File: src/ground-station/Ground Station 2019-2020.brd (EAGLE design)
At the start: 99.1 x 86.4 mm, 17 parts, among them U1 ADAFRUIT_RFM95W_LORA_RADIO

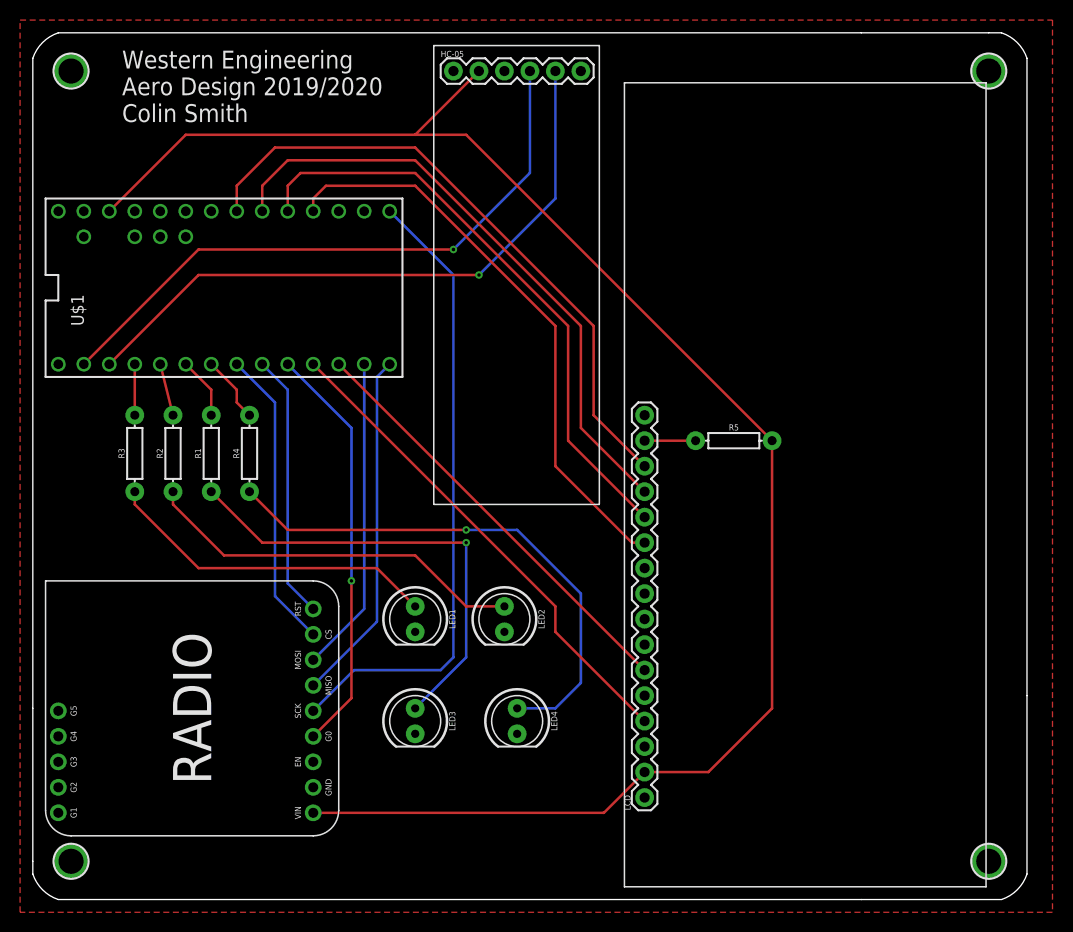
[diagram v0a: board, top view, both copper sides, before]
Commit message: Changed LCD to OLED display, changed mounting holes.
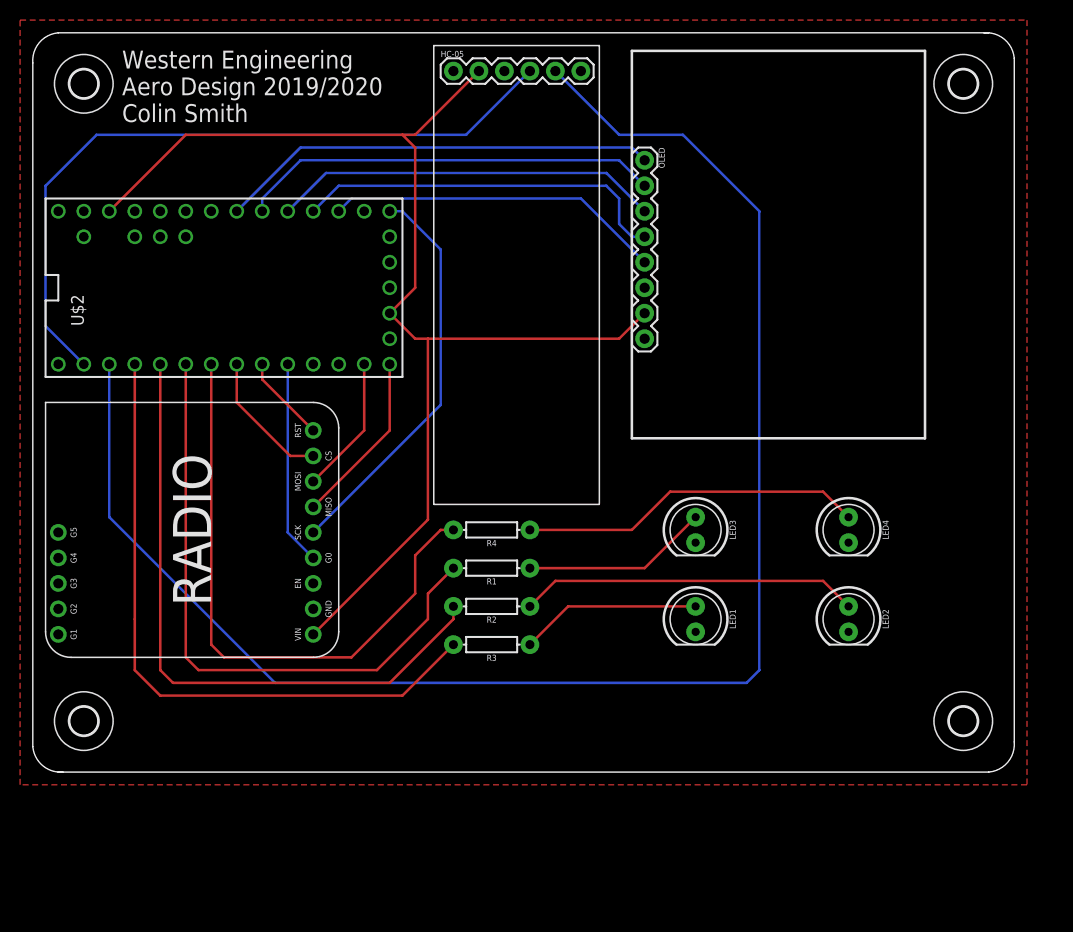
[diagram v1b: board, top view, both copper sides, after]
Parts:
- removed LCD: (no value), SparkFun-Connectors:1X16
- removed R5: 220, SparkFun-Resistors:AXIAL-0.3
- removed U$1: TEENSY_3.1-3.2_DIL+4, Teensy_3_and_LC_Series_Boards_v1.4:TEENSY_3.0-3.2&LC_DIL+4
- removed U$3, U$4, U$5: MOUNTINGHOLE2.5, microbuilder:MOUNTINGHOLE_2.5_PLATED
- added H1, H2, H3, H4: MOUNT-HOLE2.8, holes:2,8
- added OLED: (no value), SparkFun-Connectors:1X08
- U$2: value MOUNTINGHOLE2.5 -> TEENSY_3.1-3.2_ALL_PINS; device microbuilder:MOUNTINGHOLE_2.5_PLATED -> Teensy_3_and_LC_Series_Boards_v1.4:TEENSY_3.0-3.2&LC_ALL_PINS
- moved U$2 59.1 mm to (101.6, 68.6), turned to 90 degrees
- moved R3 40.3 mm to (128.3, 33.0), turned to 180 degrees
- moved LED4 38.1 mm to (163.8, 44.5)
- moved R2 35.2 mm to (128.3, 36.8), turned to 180 degrees
- moved LED2 34.3 mm to (163.8, 35.6)
- moved LED3 33.8 mm to (148.6, 44.5)
- moved R1 30.2 mm to (128.3, 40.6), turned to 180 degrees
- moved LED1 27.9 mm to (148.6, 35.6)
- moved R4 25.3 mm to (128.3, 44.5), turned to 180 degrees
- moved U1 17.8 mm to (83.8, 31.8)
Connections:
- removed net D4: LCD.11, U$1.16/A2
- removed net D5: LCD.12, U$1.17/A3
- removed net D6: LCD.13, U$1.18/A4
- removed net D7: LCD.14, U$1.19/A5
- removed net LCD_RX: LCD.4, U$1.9
- removed net LCD_TX: LCD.6, U$1.10
- removed net N$4: LCD.15, R5.P$1
- new net OLED_CLK: OLED.2, U$2.18/A4
- new net OLED_CS: OLED.5, U$2.15/A1
- new net OLED_DATA: OLED.1, U$2.19/A5
- new net OLED_DC: OLED.3, U$2.17/A3
- new net OLED_RST: OLED.4, U$2.16/A2
- new net VBAT: U$2.VBAT
- net 3.3V: now also OLED.7, U$2.3.3V, U$2.3.3V1; no longer LCD.2, R5.P$2, U$1.3.3V
- net AGND: now also U$2.AGND; no longer U$1.AGND
- net AREF: now also U$2.AREF; no longer U$1.AREF
- net CS: now also U$2.6; no longer U$1.6
- net G0: now also U$2.8; no longer U$1.8
- net GND: now also OLED.8, U$2.GND, U$2.GND1; no longer LCD.1, LCD.16, LCD.3, LCD.5, U$1.GND
- net LED1: now also U$2.2; no longer U$1.2
- net LED2: now also U$2.3; no longer U$1.3
- net LED3: now also U$2.4; no longer U$1.4
- net LED4: now also U$2.5; no longer U$1.5
- net MISO: now also U$2.12; no longer U$1.12
- net MOSI: now also U$2.11; no longer U$1.11
- net RST: now also U$2.7; no longer U$1.7
- net RX1: now also U$2.0; no longer U$1.0
- net SCK: now also U$2.13; no longer U$1.13
- net TX1: now also U$2.1; no longer U$1.1
- net VIN: now also U$2.VIN; no longer U$1.VIN
- net VUSB: now also U$2.VUSB; no longer U$1.VUSB
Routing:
- net TX1: track 64.0 -> 159.2 mm, vias 1 -> 0
- net D7: track 63.1 -> 0.00 mm
- net D6: track 61.3 -> 0.00 mm
- net LED1: track 5.08 -> 65.4 mm
- net D5: track 59.5 -> 0.00 mm
- net LED2: track 5.24 -> 64.1 mm
- net D4: track 57.7 -> 0.00 mm
- net LED3: track 6.13 -> 62.1 mm
- net LED4: track 6.66 -> 60.1 mm
- net LCD_RX: track 49.2 -> 0.00 mm
- net 3.3V: track 167.5 -> 123.7 mm
- net OLED_DATA: track 0.00 -> 43.8 mm
- net LCD_TX: track 43.1 -> 0.00 mm
- net OLED_CLK: track 0.00 -> 42.0 mm
- net OLED_DC: track 0.00 -> 38.7 mm
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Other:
- board size 99.1 x 86.4 mm -> 97.8 x 73.7 mm

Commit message: Added Cam outputs
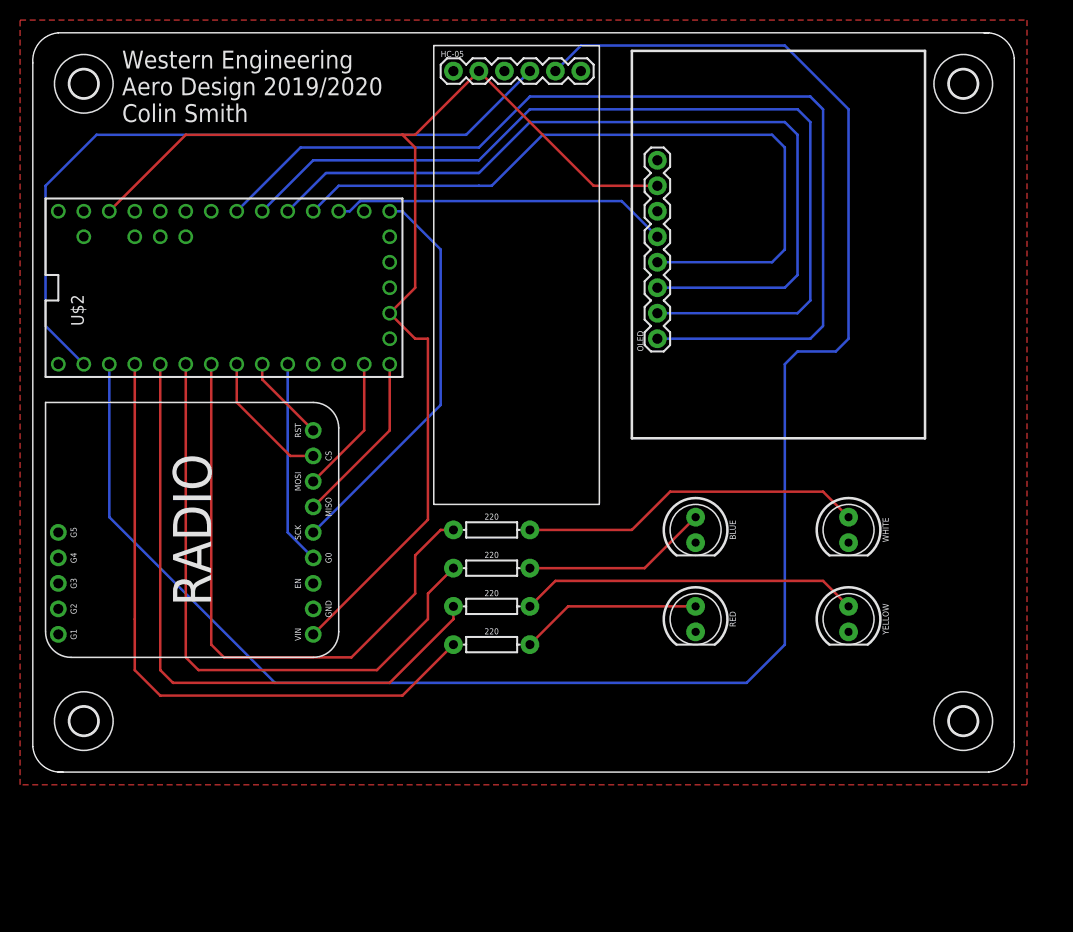
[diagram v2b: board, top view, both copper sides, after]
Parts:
- R1, R2, R3, R4: value 330 -> 220
- moved OLED 17.8 mm to (144.8, 63.5), turned to 90 degrees
- renumbered LED1 to RED, LED2 to YELLOW, LED3 to BLUE, LED4 to WHITE
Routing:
- net OLED_DATA: track 43.8 -> 102.3 mm
- net OLED_CLK: track 42.0 -> 92.9 mm
- net OLED_DC: track 38.7 -> 83.5 mm
- net OLED_RST: track 37.7 -> 74.1 mm
- net TX1: track 159.2 -> 182.1 mm
